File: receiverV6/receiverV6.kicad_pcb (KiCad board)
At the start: 4 copper layers, 52.2 x 106.5 mm, 13 parts, among them IC1 AP7361C-33E-13, J2 adafruitpwr1000, J3 S2B-PH-SM4-TB, J4 S2B-PH-SM4-TB, J5 S2B-PH-SM4-TB, J6 MM60-52B1-E1-R650, U1 Teensy4.0

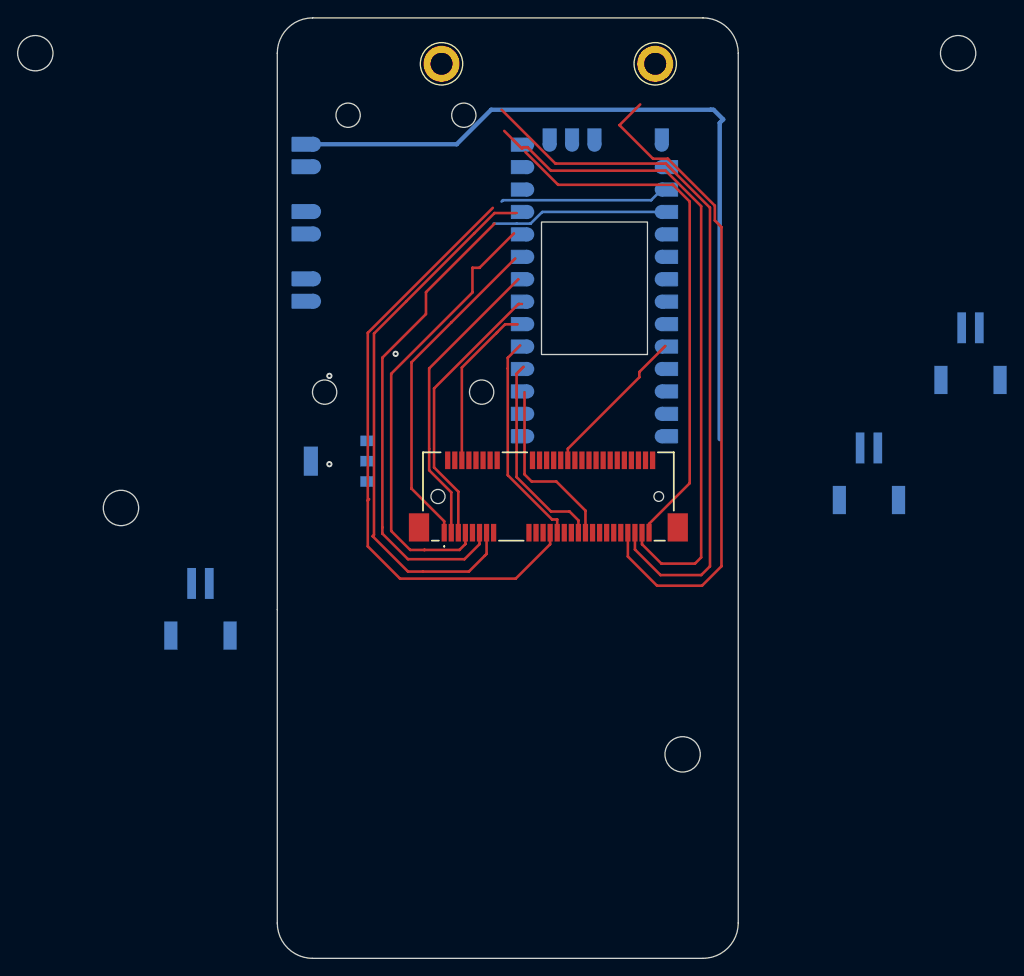
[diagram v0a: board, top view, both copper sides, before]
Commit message: add rp2350 design
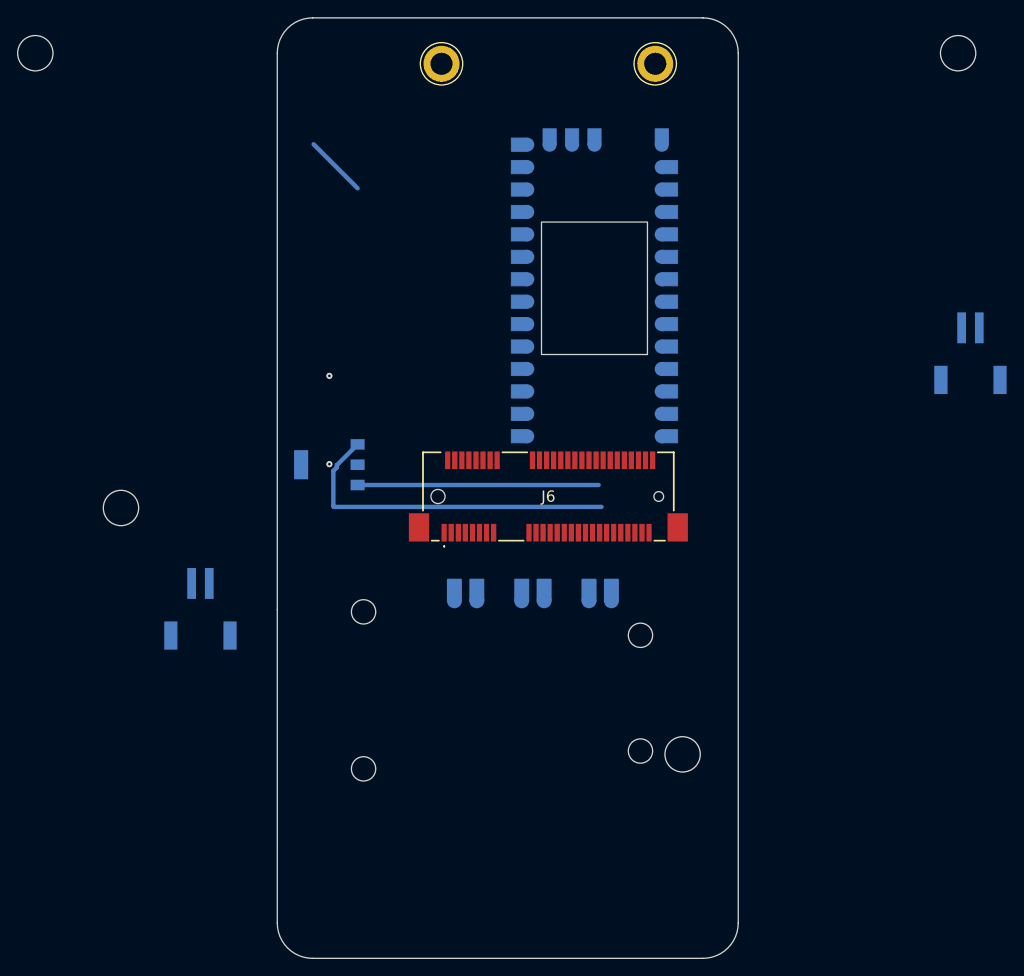
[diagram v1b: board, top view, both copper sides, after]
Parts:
- removed J5: S2B-PH-SM4-TB, JST2pin:CONN_S2B-PH-SM4-TB_JST_mod2
- moved J2 37.5 mm to (99.9, 107.3), turned to 0 degrees
- moved IC1 1.17 mm to (85.7, 91.9)
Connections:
- net /PPS renamed Net-(J6-Pad19)
- net /SX1303_RESET renamed Net-(J6-Pad22)
- U1 pad 16: (no net) -> unconnected-(U1-3V3-Pad16)
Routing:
- net /SX1261_NRESET: track 117.2 -> 0.00 mm
- net /HOST_MISO: track 80.8 -> 0.00 mm
- net /HOST_MOSI: track 74.9 -> 0.00 mm
- net /HOST_SCK: track 74.6 -> 0.00 mm
- net /RESET_GPS: track 69.5 -> 0.00 mm
- net /HOST_CSN: track 60.3 -> 0.00 mm
- net /SX1261_NSS: track 50.9 -> 0.00 mm
- net +5V: track 84.8 -> 45.6 mm
- net /SX1261_BUSY: track 37.5 -> 0.00 mm
- net /SX1261_DIO1: track 33.9 -> 0.00 mm
- net /SX1261_DIO2: track 31.4 -> 0.00 mm
- net +3.3V: track 0.00 -> 27.3 mm
- net /STANDBY_GPS: track 24.4 -> 0.00 mm
- net /GPS_RX: track 23.3 -> 0.00 mm
- net /GPS_TX: track 20.4 -> 0.00 mm
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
